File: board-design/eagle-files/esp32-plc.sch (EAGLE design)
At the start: 112 parts, among them Q1 600mA/40V, Q2 600mA/40V, Q3 500mA/300V, Q4 500mA/300V, Q5 500mA/300V, Q6 500mA/300V, Q7 500mA/300V, Q8 500mA/300V

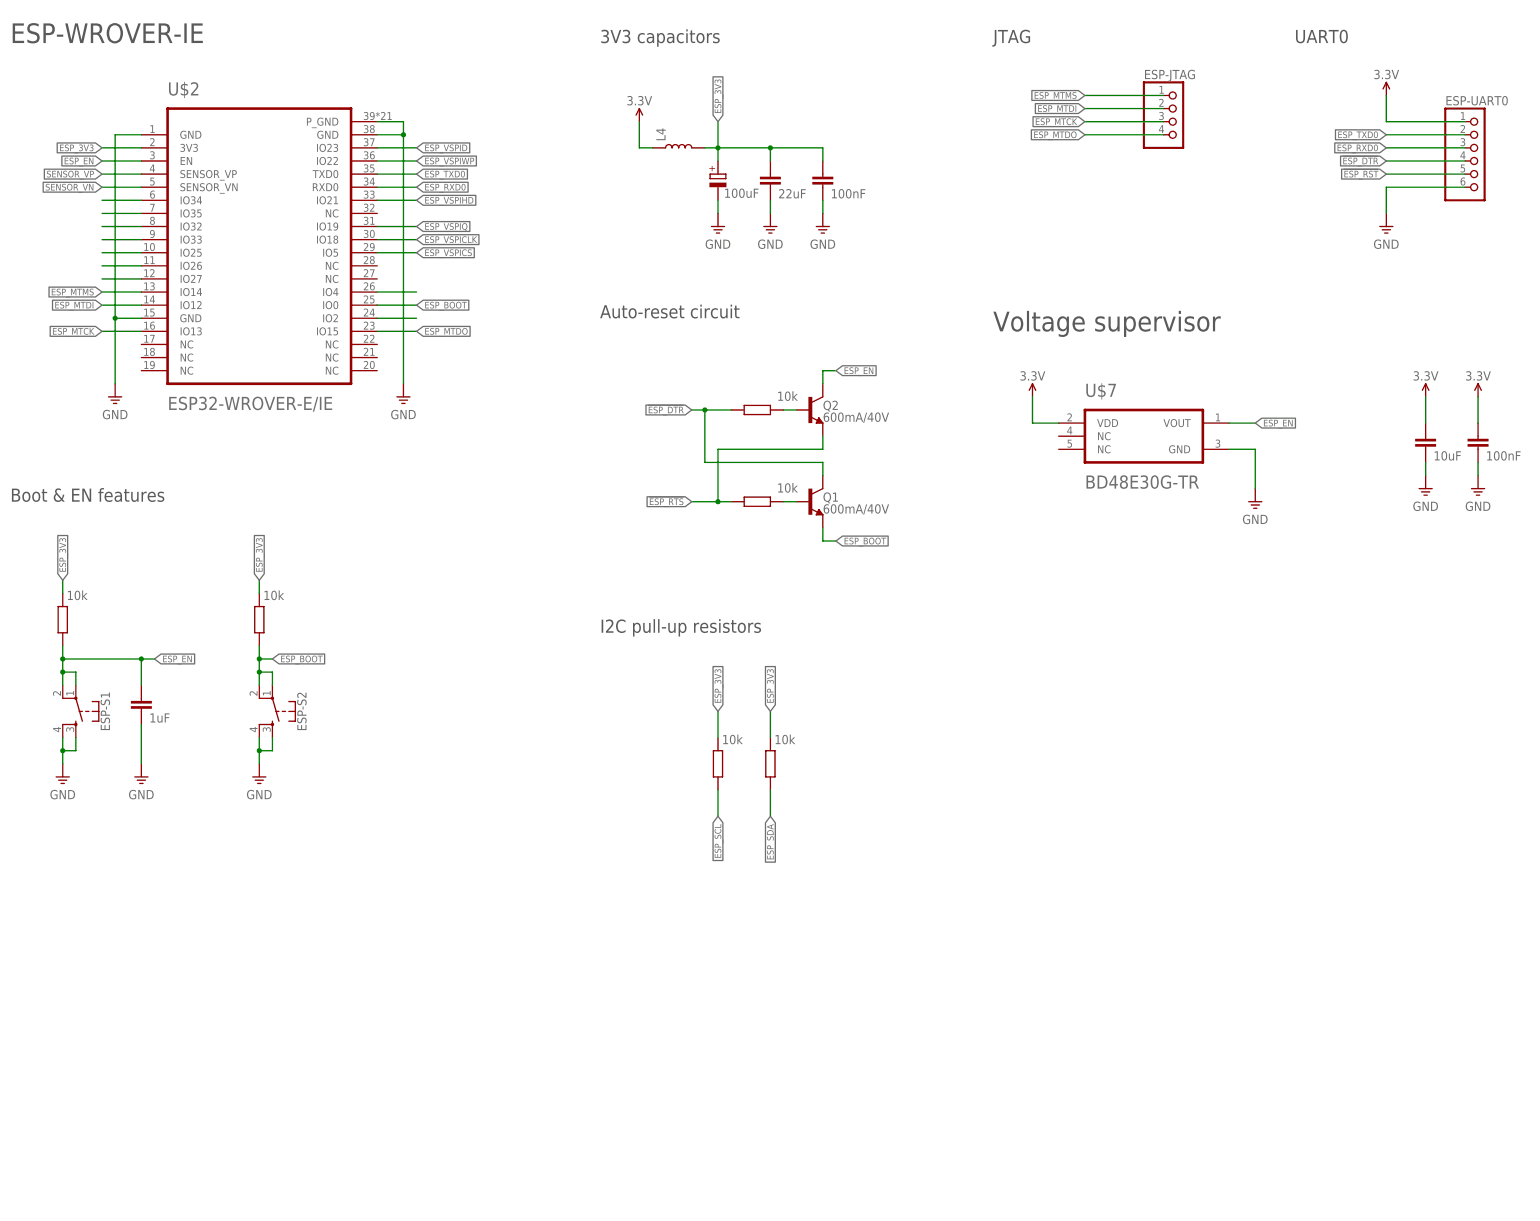
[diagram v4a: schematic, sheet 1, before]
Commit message: Logic unit schematic updated
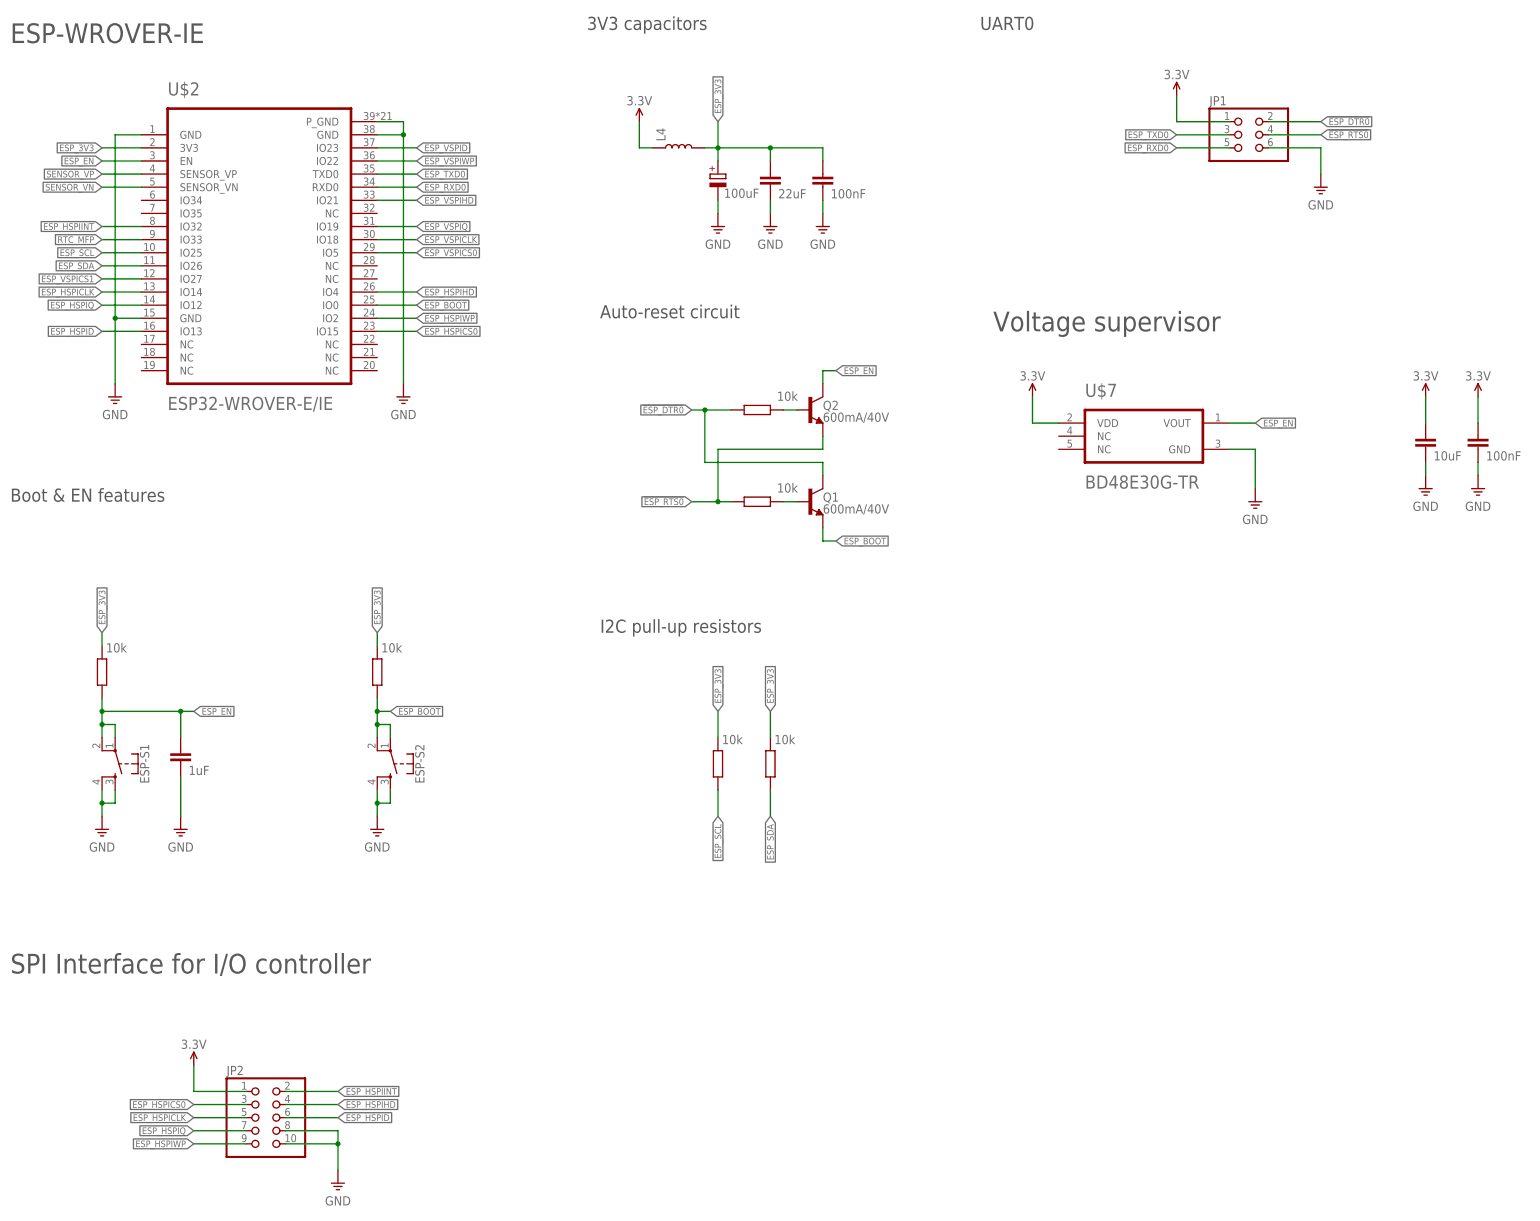
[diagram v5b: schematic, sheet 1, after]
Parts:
- removed ESP-JTAG: (no value), pinhead:PINHD-1X4
- removed ESP-UART0: (no value), pinhead:PINHD-1X6
- added JP1: (no value), pinhead:PINHD-2X3
- added JP2: (no value), pinhead:PINHD-2X5
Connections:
- removed net !ESP_DTR: ESP-R1.1, ESP-UART0.4, Q1.C
- removed net !ESP_RST: ESP-UART0.5
- removed net !ESP_RTS: ESP-R2.1, Q2.E
- removed net EEPROM_C: U$1.C
- removed net EEPROM_D: U$1.D
- removed net EEPROM_HOLD: U$1.!HOLD
- removed net EEPROM_Q: U$1.Q
- removed net EEPROM_S: U$1.!S
- removed net EEPROM_W: U$1.!W
- removed net EERAM_CS: U$5.!CS
- removed net EERAM_HOLD: U$5.!HOLD
- removed net EERAM_SCK: U$5.SCK
- removed net EERAM_SI: U$5.SI
- removed net EERAM_SO: U$5.SO
- removed net ESP_MTCK: ESP-JTAG.3, U$2.IO13
- removed net ESP_MTDI: ESP-JTAG.2, U$2.IO12
- removed net ESP_MTDO: ESP-JTAG.4, U$2.IO15
- removed net ESP_MTMS: ESP-JTAG.1, U$2.IO14
- removed net ESP_VSPICS: U$2.IO5
- removed net N$14: U$2.IO27
- removed net N$15: U$2.IO26
- removed net N$16: U$2.IO25
- removed net N$17: U$2.IO33
- removed net N$18: U$2.IO32
- removed net N$19: U$2.IO35
- removed net N$20: U$2.IO34
- removed net N$24: U$3.SCL
- removed net N$25: U$3.SDA
- removed net N$27: U$2.IO4
- removed net N$31: U$2.IO2
- new net !ESP_DTR0: ESP-R1.1, JP1.2, Q1.C
- new net !ESP_RTS0: ESP-R2.1, JP1.4, Q2.E
- new net ESP_HSPICLK: JP2.5, U$2.IO14
- new net ESP_HSPICS0: JP2.3, U$2.IO15
- new net ESP_HSPID: JP2.6, U$2.IO13
- new net ESP_HSPIHD: JP2.4, U$2.IO4
- new net ESP_HSPIINT: JP2.2, U$2.IO32
- new net ESP_HSPIQ: JP2.7, U$2.IO12
- new net ESP_HSPIWP: JP2.9, U$2.IO2
- new net ESP_VSPICS0: U$1.!S, U$2.IO5
- new net ESP_VSPICS1: U$2.IO27, U$5.!CS
- net 3.3V: now also JP1.1, JP2.1; no longer ESP-UART0.1
- net ESP_RXD0: now also JP1.5; no longer ESP-UART0.3
- net ESP_SCL: now also U$2.IO25, U$3.SCL
- net ESP_SDA: now also U$2.IO26, U$3.SDA
- net ESP_TXD0: now also JP1.3; no longer ESP-UART0.2
- net ESP_VSPICLK: now also U$1.C, U$5.SCK
- net ESP_VSPID: now also U$1.Q, U$5.SO
- net ESP_VSPIHD: now also U$1.!HOLD, U$5.!HOLD
- net ESP_VSPIQ: now also U$1.D, U$5.SI
- net ESP_VSPIWP: now also U$1.!W
- net GND: now also JP1.6, JP2.10, JP2.8; no longer ESP-UART0.6
- net RTC_MFP: now also U$2.IO33
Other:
- note added: "Not enough ESP32 pins for MAX24385 and EC20 connections"
- note added: "Notes: The cases of capacitors has to be determined, only the values being relevant at the moment. The cases and characteristics of inductors and diodes have yet to be determined. They were selected randomly for circuit showing purposes. Warning: Not enough ESP32 pins for UART connections (RS-485 and LTE). Auxiliary uC needed. Possibility to include the ethernet module as well (increased complexi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"
- note added: "SPI Interface for I/O controller"
- note removed: "JTAG"
- note removed: "Notes: The cases of capacitors has to be determined, only the values being relevant at the moment. The cases and characteristics of inductors and diodes have yet to be determined. They were selected randomly for circuit showing purposes. This is a draft!"
- moved on the sheet: ESP-S1, ESP-S2

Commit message: PLC Update
Added Ethernet module.

Signed-off-by: Nicolae-Andrei Vasile <vasilenicolaeandrei@gmail.com>
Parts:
- added ETH-RJ45-C1, ETH-VDDCR-C1: 1uF, rcl:C-EUC0402
- added ETH-RJ45-R1, ETH-RJ45-R2, ETH-RJ45-R3, ETH-RJ45-R4: 49.9R, rcl:R-EU_R0402
- added ETH-RJ45-R10, ETH-RJ45-R11: 10k, rcl:R-EU_R0402
- added ETH-RJ45-R5, ETH-RJ45-R6: 1k, rcl:R-EU_R0402
- added ETH-RJ45-R8: 12.1R (1%), rcl:R-EU_R0402
- added ETH-RJ45-R9: 500R, rcl:R-EU_R0402
- added ETH-VDD1A-C1, ETH-VDD2A-C1: 10uF, rcl:C-EUC0402
- added ETH-VDD1A-C2, ETH-VDD2A-C2, ETH-VDDIO-C2: 100nF, rcl:C-EUC0402
- added ETH-VDD2A-C3, ETH-VDD2A-C4, ETH-VDD2A-C5: 20pF, rcl:C-EUC0402
- added ETH-VDDCR-C2: 470pF, rcl:C-EUC0402
- added ETH-VDDIO-C1: 22uF, rcl:CPOL-EUC/6032-28R
- added L2: (no value), SparkFun-Coils:INDUCTOR
- added U$105: LAN8720A-CP, my-MicrochipTechnology:LAN8720A-CP
- added U$111: 7499010121A, my-WurthElektronik:7499010121A
- added U$123: ECS-250-20-30B-AEN-TR, my-ECSInc:ECS-250-20-30B-AEN-TR
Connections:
- new net ETH_NRST: ETH-RJ45-R10.1, ETH-VDD2A-C5.1, U$105.NRST
- new net ETH_RJ45_LED1: ETH-RJ45-R5.2, U$105.LED1/!REGOFF
- new net ETH_RJ45_LED2: ETH-RJ45-R11.2, ETH-RJ45-R6.2, U$105.LED2/!NINTSEL
- new net ETH_RJ45_RXN: ETH-RJ45-R4.2, U$105.RXN, U$111.RD-
- new net ETH_RJ45_RXP: ETH-RJ45-R3.2, U$105.RXP, U$111.RD+
- new net ETH_RJ45_TXN: ETH-RJ45-R2.2, U$105.TXN, U$111.TD-
- new net ETH_RJ45_TXP: ETH-RJ45-R1.2, U$105.TXP, U$111.TD+
- new net ETH_VDD: ETH-RJ45-C1.1, ETH-RJ45-R1.1, ETH-RJ45-R10.2, ETH-RJ45-R2.1, ETH-RJ45-R3.1, ETH-RJ45-R4.1, ETH-VDD1A-C1.1, ETH-VDD1A-C2.1, ETH-VDD2A-C1.1, ETH-VDD2A-C2.1, ETH-VDDIO-C1.+, ETH-VDDIO-C2.1, L2.2, U$105.VDD1A, U$105.VDD2A, U$105.VDDIO, U$111.RCT, U$111.TCT
- new net ETH_VDDCR: ETH-VDDCR-C1.1, ETH-VDDCR-C2.1, U$105.VDDCR
- new net ETH_XTAL1: ETH-VDD2A-C3.1, U$105.XTAL1/CLKIN, U$123.XTAL1
- new net ETH_XTAL2: ETH-RJ45-R9.1, U$105.XTAL2
- new net N$20: ETH-RJ45-R8.2, U$105.RBIAS
- new net N$27: U$105.RXER/!PHYAD0
- new net N$31: U$105.CRS_DV/!MODE2
- new net N$34: U$105.MDIO
- new net N$35: U$105.MDC
- new net N$36: ETH-RJ45-R5.1, U$111.GREEN+
- new net N$37: U$105.TXEN
- new net N$38: ETH-RJ45-R6.1, U$111.YELLOW+
- new net N$39: U$105.TXD0
- new net N$40: U$105.TXD1
- new net N$41: U$105.RXD1/!MODE1
- new net N$42: U$105.RXD0/!MODE0
- new net N$43: U$105.NINT/REFCLKO
- new net N$44: ETH-RJ45-R9.2, ETH-VDD2A-C4.1, U$123.XTAL2
- net 3.3V: now also L2.1
- net GND: now also ETH-RJ45-C1.2, ETH-RJ45-R11.1, ETH-RJ45-R8.1, ETH-VDD1A-C1.2, ETH-VDD1A-C2.2, ETH-VDD2A-C1.2, ETH-VDD2A-C2.2, ETH-VDD2A-C3.2, ETH-VDD2A-C4.2, ETH-VDD2A-C5.2, ETH-VDDCR-C1.2, ETH-VDDCR-C2.2, ETH-VDDIO-C1.-, ETH-VDDIO-C2.2, U$105.P_GND, U$111.8, U$111.GREEN-, U$111.SHIELD@1, U$111.SHIELD@2, U$111.YELLOW-, U$123.GND
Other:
- note added: "25MHz crystal"
- note added: "ETHERNET LM7820A"
- note added: "RJ45LAN transformer"
- note added: "VDD capacitors"
- note added: "nRST pull-up"
- note removed: "Not enough ESP32 pins for MAX24385 and EC20 connections"
- moved on the sheet: JP1, JP2, JP4, U$10, U$11, U$7

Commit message: PLC board design
Verifications and improvements of the hardware design.

Signed-off-by: Nicolae-Andrei Vasile <vasilenicolaeandrei@gmail.com>
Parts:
- removed C1: 1nF/1kV, rcl:C-EUC0805
- removed C4-RTC: 100pF, rcl:C-EUC0402
- removed D2: 3A/40V/500mV, SparkFun-DiscreteSemi:DIODE-SCHOTTKY-B340A
- removed EEPROM-C2, ETH-VDD1A-C1, ETH-VDD2A-C1: 10uF, rcl:C-EUC0402
- removed ETH-RJ45-C1, ETH-VDDCR-C1: 1uF, rcl:C-EUC0402
- removed ETH-RJ45-R1, ETH-RJ45-R2, ETH-RJ45-R3, ETH-RJ45-R4: 49.9R, rcl:R-EU_R0402
- removed ETH-RJ45-R5, ETH-RJ45-R6, R1-RTC1: 1k, rcl:R-EU_R0402
- removed ETH-RJ45-R9: 500R, rcl:R-EU_R0402
- removed ETH-VDD1A-C2, ETH-VDD2A-C2, ETH-VDDIO-C2: 100nF, rcl:C-EUC0402
- removed ETH-VDDCR-C2: 470pF, rcl:C-EUC0402
- removed ETH-VDDIO-C1, LTE-VBAT-C10: 22uF, rcl:CPOL-EUC/6032-28R
- removed G1: CR2032H, battery:CR2032H
- removed JP4: (no value), pinhead:PINHD-1X2
- removed R1: 42/2kV, rcl:R-EU_R0805
- removed R1-RTC: 10K, rcl:R-EU_R0402
- removed RS-R1: 120, rcl:R-EU_R0402
- removed U$10: ESDA6V1P6, my-STMicroelectronics:ESDA6V1P6
- removed U$11: MAX3485CSA+T, my-MaximIntegrated:MAX3485CSA+T
- removed U$111: 7499010121A, my-WurthElektronik:7499010121A
- removed U$123: ECS-250-20-30B-AEN-TR, my-ECSInc:ECS-250-20-30B-AEN-TR
- removed U$3: MCP7940N-I/SN, my-Microchip-Technology:MCP7940N-I/SN
- removed U$4: ECS-.327-12.5-12QS-TR, my-ECSInc:ECS-.327-12.5-12QS-TR
- removed U$9: 104224-0820, my-Molex:104224-0820
- added EEPROM-C0, RTC-C0: 10uF, rcl:C-EUC0402
- added EEPROM_IC: M95M01-DWDW3TP/K, my-STMicroelectronics:M95M01-DWDW3TP/K
- added ETH-C0, ETH-C3, ETH-C6, ETH-C9, RS-C0: 22uF, rcl:CPOL-EUC/6032-28R
- added ETH-C1, ETH-C11, ETH-C4, ETH-C7, ETHC-9: 1uF, rcl:C-EUC0402
- added ETH-C10: 470pF, rcl:C-EUC0402
- added ETH-C2, ETH-C5, ETH-C8: 100nF, rcl:C-EUC0402
- added ETH-R2, ETH-R3, ETH-R4, ETH-R5: 49.9, rcl:R-EU_R0402
- added ETH-R6, ETH-R7: 270, rcl:R-EU_R0402
- added ETH-RJ45-R12, ETH-RJ45-R7: 330, rcl:R-EU_R0402
- added ETH_CRYSTAL: FL2500213Z, my-DiodesIncorporated:FL2500213Z
- added ETH_RJ45: 7499010121A, my-WurthElektronik:7499010121A
- added LTE-UART-R11, LTE-UART-R13: 4.7K, rcl:R-EU_R0402
- added LTE-UART-R12, LTE-UART-R14: 47K, rcl:R-EU_R0402
- added LTE_IC: EC20CEFASG-MINIPCIE, my-Quectel:EC20CEFASG-MINIPCIE
- added LTE_USIM: 104224-0820, my-Molex:104224-0820
- added MAX_PINH0: A, pinhead:PINHD-1X1
- added MAX_PINH1: B, pinhead:PINHD-1X1
- added MAX_PINH2: GND, pinhead:PINHD-1X1
- added Q10, Q9: 500mA/300V, SparkFun-DiscreteSemi:TRANS_NPN-MMBTA42
- added RS_IC: MAX3485CSA+T, my-MaximIntegrated:MAX3485CSA+T
- added RTC-D0: 3A/80V, my-Vishay:V3PM6-M3/H
- added RTC-R0: 1k, rcl:R-EU_R0402
- added RTC-R2: 10K, rcl:R-EU_R0402
- added RTC_BAT: SMTU2032-C, my-Renata:SMTU2032-C
- added RTC_CRYSTAL: ECS-.327-7-34B-C-TR, my-ECSInc:ECS-.327-7-34B-C-TR
- added RTC_IC: MCP7940N-I/SN, my-Microchip-Technology:MCP7940N-I/SN
- added U$101, U$102: 20, my-Vishay:SMM02040C2009FB000
- added U$139: GREEN, my-WurthElektronik:150060XS75000
- added U$140: RED, my-WurthElektronik:150060XS75000
- ETH-C12, ETH-C13: value 20pF -> 25pF
- ETH-VDD2A-C5: value 20pF -> 1nF
- L2, L3: value (none) -> TBD
- LTE-VBAT-C9: value 22uF -> 10nF; device rcl:CPOL-EUC/6032-28R -> rcl:C-EUC0402
- RTC-C2, RTC-C3: value 15pF -> 10pF
- RTC-C4: value 10uF -> 100pF
- U$1: value M95M01-DWMN3TP/K -> VESD16A2-03G-G3-08; device my-STMicroelectronics:M95M01-DWMN3TP/K -> my-Vishay:VESD16A2-03G-G3-08
- U$6: value EC20CEFASG-MINIPCIE -> ESDALC6V1-5P6; device my-Quectel:EC20CEFASG-MINIPCIE -> my-STMicroelectronics:ESDALC6V1-5P6
- renumbered ETH-RJ45-R10 to ETH-R1, ETH-RJ45-R8 to ETH-R0, ETH-VDD2A-C3 to ETH-C12, ETH-VDD2A-C4 to ETH-C13, U$105 to ETH_IC
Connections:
- net N$27 renamed ETH_RXER
- net N$31 renamed ETH_CRS_DV
- net N$34 renamed ETH_MDIO
- net N$35 renamed ETH_MDC
- net N$37 renamed ETH_TXEN
- net N$39 renamed ETH_TXD0
- net N$40 renamed ETH_TXD1
- net N$41 renamed ETH_RXD1
- net N$42 renamed ETH_RXD0
- net N$43 renamed ETH_NINT
- removed net N$28: JP4.2, RS-R1.2, U$11.A
- removed net N$32: JP4.1, RS-R1.1, U$11.B
- removed net N$36: ETH-RJ45-R5.1, U$111.GREEN+
- removed net N$38: ETH-RJ45-R6.1, U$111.YELLOW+
- removed net N$44: ETH-C13.1, ETH-RJ45-R9.2, U$123.XTAL2
- removed net USIM_DATA: U$10.I/O4
- new net LTE_PWRKEY: LTE-VBAT-C9.1, LTE_IC.PWRKEY, Q9.C
- new net LTE_RESET_N: LTE_IC.RESET_N, Q10.C
- new net LTE_STATUS: LTE_IC.STATUS
- new net MAX_A: RS_IC.B, U$102.1
- new net MAX_B: RS_IC.A, U$101.1
- new net N$14: MAX_PINH0.1, U$1.I/O2, U$102.2
- new net N$15: MAX_PINH1.1, U$1.I/O1, U$101.2
- new net N$16: ETH-RJ45-R7.1, U$139.1
- new net N$17: ETH-RJ45-R12.1, U$140.1
- new net N$18: ETH-R6.2, ETH_RJ45.GREEN-
- new net N$19: ETH-R7.2, ETH_RJ45.YELLOW-
- new net N$21: LTE-UART-R11.1, LTE-UART-R12.2, Q9.B
- new net N$24: LTE-UART-R11.2
- new net N$25: LTE-UART-R13.1, LTE-UART-R14.2, Q10.B
- new net N$26: LTE-UART-R13.2
- net 3.3V: now also EEPROM-C0.1, EEPROM_IC.VCC, ETH-C9.+, RS-C0.+, RS_IC.VCC, RTC-C0.1, RTC-R2.2, RTC_IC.VCC; no longer EEPROM-C2.1, R1-RTC.2, RTC-C4.1, U$1.VCC, U$11.VCC, U$3.VCC
- net ESP_SCL: now also RTC_IC.SCL; no longer U$3.SCL
- net ESP_SDA: now also RTC_IC.SDA; no longer U$3.SDA
- net ESP_VSPICLK: now also EEPROM_IC.C; no longer U$1.C
- net ESP_VSPICS0: now also EEPROM_IC.!S; no longer U$1.!S
- net ESP_VSPID: now also EEPROM_IC.Q; no longer U$1.Q
- net ESP_VSPIHD: now also EEPROM_IC.!HOLD; no longer U$1.!HOLD
- net ESP_VSPIQ: now also EEPROM_IC.D; no longer U$1.D
- net ESP_VSPIWP: now also EEPROM_IC.!W; no longer U$1.!W
- net ETH_RJ45_LED1: now also ETH_RJ45.GREEN+; no longer ETH-RJ45-R5.2
- net ETH_RJ45_LED2: now also ETH_RJ45.YELLOW+; no longer ETH-RJ45-R6.2
- net ETH_RJ45_RXN: now also ETH-R5.2, ETH_RJ45.RD-; no longer ETH-RJ45-R4.2, U$111.RD-
- net ETH_RJ45_RXP: now also ETH-R4.2, ETH_RJ45.RD+; no longer ETH-RJ45-R3.2, U$111.RD+
- net ETH_RJ45_TXN: now also ETH-R3.2, ETH_RJ45.TD-; no longer ETH-RJ45-R2.2, U$111.TD-
- net ETH_RJ45_TXP: now also ETH-R2.2, ETH_RJ45.TD+; no longer ETH-RJ45-R1.2, U$111.TD+
- net ETH_VDD: now also ETH-C0.+, ETH-C1.1, ETH-C11.1, ETH-C2.1, ETH-C3.+, ETH-C4.1, ETH-C5.1, ETH-C6.+, ETH-C7.1, ETH-C8.1, ETH-R2.1, ETH-R3.1, ETH-R4.1, ETH-R5.1, ETH_RJ45.RCT, ETH_RJ45.TCT; no longer ETH-RJ45-C1.1, ETH-RJ45-R1.1, ETH-RJ45-R2.1, ETH-RJ45-R3.1, ETH-RJ45-R4.1, ETH-VDD1A-C1.1, ETH-VDD1A-C2.1, ETH-VDD2A-C1.1, ETH-VDD2A-C2.1, ETH-VDDIO-C1.+, ETH-VDDIO-C2.1, U$111.RCT, U$111.TCT
- net ETH_VDDCR: now also ETH-C10.1, ETHC-9.1; no longer ETH-VDDCR-C1.1, ETH-VDDCR-C2.1
- net ETH_XTAL1: now also ETH_CRYSTAL.XTAL1; no longer U$123.XTAL1
- net ETH_XTAL2: now also ETH-C13.1, ETH_CRYSTAL.XTAL2; no longer ETH-RJ45-R9.1
- net GND: now also EEPROM-C0.2, EEPROM_IC.VSS, ETH-C0.-, ETH-C1.2, ETH-C10.2, ETH-C11.2, ETH-C2.2, ETH-C3.-, ETH-C4.2, ETH-C5.2, ETH-C6.-, ETH-C7.2, ETH-C8.2, ETH-C9.-, ETH-R6.1, ETH-R7.1, ETH-RJ45-R12.2, ETH-RJ45-R7.2, ETHC-9.2, ETH_CRYSTAL.GND, ETH_RJ45.8, ETH_RJ45.SHIELD@1, ETH_RJ45.SHIELD@2, LTE-UART-R12.1, LTE-UART-R14.1, LTE-VBAT-C9.2, LTE_IC.GND, MAX_PINH2.1, Q10.E, Q9.E, RS-C0.-, RS_IC.GND, RTC-C0.2, RTC_BAT.2, RTC_IC.VSS, U$1.GND; no longer C1.1, C4-RTC.2, EEPROM-C2.2, ETH-RJ45-C1.2, ETH-VDD1A-C1.2, ETH-VDD1A-C2.2, ETH-VDD2A-C1.2, ETH-VDD2A-C2.2, ETH-VDDCR-C1.2, ETH-VDDCR-C2.2, ETH-VDDIO-C1.-, ETH-VDDIO-C2.2, G1.-, LTE-VBAT-C10.-, LTE-VBAT-C9.-, R1.2, U$1.VSS, U$10.GND@1, U$10.GND@2, U$11.GND, U$111.8, U$111.GREEN-, U$111.SHIELD@1, U$111.SHIELD@2, U$111.YELLOW-, U$123.GND, U$3.VSS
- net LTE_AP_READY: now also LTE_IC.AP_READY; no longer U$6.AP_READY
- net LTE_DBG_RXD: now also LTE_IC.DBG_RXD; no longer U$6.DBG_RXD
- net LTE_DBG_TXD: now also LTE_IC.DBG_TXD; no longer U$6.DBG_TXD
- net LTE_DTR: now also LTE_IC.DTR; no longer U$6.DTR
- net LTE_RI: now also LTE_IC.RI; no longer U$6.RI
- net LTE_RXD: now also LTE_IC.RXD; no longer U$6.RXD
- net LTE_TXD: now also LTE_IC.TXD; no longer U$6.TXD
- net LTE_USIM_CLK: now also LTE_IC.USIM_CLK; no longer U$6.USIM_CLK
- net LTE_USIM_DATA: now also LTE_IC.USIM_DATA; no longer U$6.USIM_DATA
- net LTE_USIM_GND: now also LTE-USIM-C1.2, LTE_IC.USIM_GND, LTE_USIM.GND; no longer LTE-USIM-C1.1, U$6.USIM_GND, U$9.GND
- net LTE_USIM_RST: now also LTE_IC.USIM_RST; no longer U$6.USIM_RST
- net LTE_USIM_VDD: now also LTE-USIM-C1.1, LTE_IC.USIM_VDD, LTE_USIM.VCC, U$6.I/O3; no longer LTE-USIM-C1.2, U$10.I/O1, U$6.USIM_VDD, U$9.VCC
- net LTE_VBAT: now also LTE_IC.VBAT_BB, LTE_IC.VBAT_RF; no longer LTE-VBAT-C10.+, LTE-VBAT-C9.+, U$6.VBAT_BB, U$6.VBAT_RF
- net LTE_VDD_EXT: now also LTE_IC.VDD_EXT; no longer U$6.VDD_EXT
- net N$6: now also RTC-D0.2, RTC-R0.2; no longer D2.C, R1-RTC1.2
- net N$7: now also RTC-D0.1, RTC_BAT.1; no longer D2.A, G1.+
- net P$1: no longer C1.2, R1.1
- net RS-DE: now also RS_IC.DE; no longer U$11.DE
- net RS-DI: now also RS_IC.DI, U$139.2; no longer U$11.DI
- net RS-RE: now also RS_IC.!RE; no longer U$11.!RE
- net RS-RO: now also RS_IC.RO, U$140.2; no longer U$11.RO
- net RTC_MFP: now also RTC-R2.1, RTC_IC.MFP; no longer U$3.MFP
- net RTC_VBAT: now also RTC-C4.1, RTC-R0.1, RTC_IC.VBAT; no longer C4-RTC.1, R1-RTC.1, R1-RTC1.1, U$3.VBAT
- net RTC_X1: now also RTC_CRYSTAL.1, RTC_IC.X1; no longer U$3.X1, U$4.P$1
- net RTC_X2: now also RTC_CRYSTAL.2, RTC_IC.X2; no longer U$3.X2, U$4.P$2
- net USIM_CLK: now also LTE_USIM.CLK, U$6.I/O1; no longer U$10.I/O3, U$9.CLK
- net USIM_I/O: now also LTE_USIM.I/O, U$6.I/O2; no longer U$9.I/O
- net USIM_RST: now also LTE_USIM.RST, U$6.I/O5; no longer U$10.I/O2, U$9.RST
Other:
- note added: "(U)SIM card holder (ok)"
- note added: "25MHz crystal (ok)"
- note added: "32kHz crystal (ok)"
- note added: "Back-up supply (ok)"
- note added: "ESD Protection (ok)"
- note added: "ETHERNET LM7820A (ok)"
- note added: "LTE EC20 R2.1 (ok)"
- note added: "Power ON/OFF scenarios"
- note added: "RJ45LAN transformer (ok)"
- note added: "RS-422/RS-485 Interface IC (ok)"
- note added: "Real-Time Clock (ok)"
- note added: "SPI bus EEPROM (ok)"
- note added: "SPI bus EERAM (EOL - another needed)"
- note added: "VDD capacitors (ok)"
- note added: "nRST pull-up (ok)"
- note removed: "(U)SIM card holder"
- note removed: "25MHz crystal"
- note removed: "32kHz crystal"
- note removed: "Back-up supply"
- note removed: "ESP32 - EC20 UART connection: EC20 ESP32 ___________ ___________ RXD <- - - - - - - - - - TXD TXD - - - - - - - - - -> RXD RI - - - - - - - - - -> EINT DTR <- - - - - - - - - - GPIO AP_READY <- - - - - - - - - - GPIO GND - - - - - - - - - - - GND"
- note removed: "ETHERNET LM7820A"
- note removed: "LTE EC20 R2.1"
- note removed: "RJ45LAN transformer"
- note removed: "RS-422/RS-485 Interface IC"
- note removed: "Real-Time Clock"
- note removed: "SPI bus EEPROM"
- note removed: "SPI bus EERAM"
- note removed: "Surge protection"
- note removed: "VDD capacitors"
- note removed: "nRST pull-up"
- moved on the sheet: L2
